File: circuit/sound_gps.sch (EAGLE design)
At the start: 12 parts, among them CON1 MA02-1, IC1 7805TV

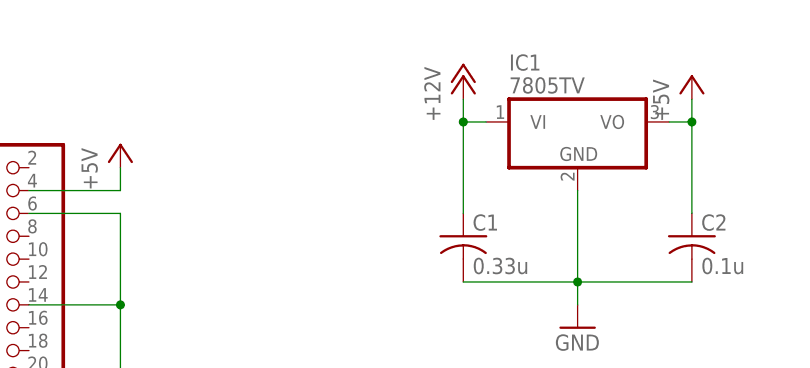
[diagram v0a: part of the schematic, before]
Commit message: スイッチを追加した
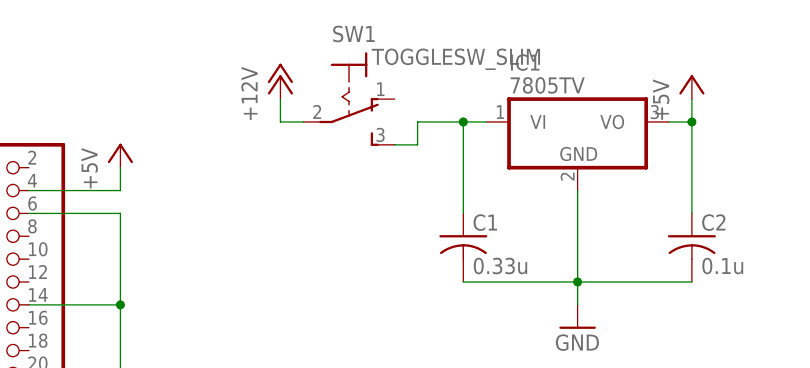
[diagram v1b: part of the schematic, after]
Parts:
- added SW1: TOGGLESW_SLIM, Passive_Robotech:TOGGLESW_SLIM
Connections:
- new net N$3: C1.1, IC1.VI, SW1.S
- net +12V: now also SW1.P; no longer C1.1, IC1.VI
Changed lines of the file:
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@@
 <part name="GND6" library="supply1" deviceset="GND" device=""/>
 <part name="R1" library="Passive_Robotech" deviceset="R" device="-1608" value="10k"/>
+<part name="SW1" library="Passive_Robotech" deviceset="TOGGLESW_SLIM" device=""/>
 </parts>
 <sheets>
@@
 <instance part="JP1" gate="A" x="-66.04" y="45.72"/>
 <instance part="IC1" gate="A1" x="0" y="73.66"/>
-<instance part="P+1" gate="1" x="-12.7" y="78.74"/>
+<instance part="P+1" gate="1" x="-33.02" y="78.74"/>
 <instance part="P+2" gate="1" x="12.7" y="78.74"/>
 <instance part="GND1" gate="1" x="0" y="50.8"/>
@@
 <instance part="GND6" gate="1" x="-27.94" y="10.16"/>
 <instance part="R1" gate="G$1" x="-27.94" y="33.02" rot="R90"/>
+<instance part="SW1" gate="G$1" x="-25.4" y="76.2" rot="R270"/>
 </instances>
 <busses>
@@
 <net name="+12V" class="0">
 <segment>
-<pinref part="P+1" gate="1" pin="+12V"/>
-<wire x1="-12.7" y1="76.2" x2="-12.7" y2="73.66" width="0.1524" layer="91"/>
-<pinref part="IC1" gate="A1" pin="VI"/>
-<wire x1="-12.7" y1="73.66" x2="-10.16" y2="73.66" width="0.1524" layer="91"/>
-<wire x1="-12.7" y1="73.66" x2="-12.7" y2="63.5" width="0.1524" layer="91"/>
-<junction x="-12.7" y="73.66"/>
-<pinref part="C1" gate="G$1" pin="1"/>
-</segment>
-<segment>
 <pinref part="POWER" gate="G$1" pin="3"/>
 <pinref part="P+4" gate="1" pin="+12V"/>
 <wire x1="-60.96" y1="-5.08" x2="-55.88" y2="-5.08" width="0.1524" layer="91"/>
 <wire x1="-55.88" y1="-5.08" x2="-55.88" y2="-2.54" width="0.1524" layer="91"/>
+</segment>
+<segment>
+<pinref part="P+1" gate="1" pin="+12V"/>
+<wire x1="-33.02" y1="76.2" x2="-33.02" y2="73.66" width="0.1524" layer="91"/>
+<pinref part="SW1" gate="G$1" pin="P"/>
+<wire x1="-33.02" y1="73.66" x2="-30.48" y2="73.66" width="0.1524" layer="91"/>
 </segment>
 </net>
@@
 </segment>
 </net>
+<net name="N$3" class="0">
+<segment>
+<pinref part="IC1" gate="A1" pin="VI"/>
+<wire x1="-12.7" y1="73.66" x2="-10.16" y2="73.66" width="0.1524" layer="91"/>
+<wire x1="-12.7" y1="73.66" x2="-12.7" y2="63.5" width="0.1524" layer="91"/>
+<pinref part="C1" gate="G$1" pin="1"/>
+<pinref part="SW1" gate="G$1" pin="S"/>
+<wire x1="-20.32" y1="71.12" x2="-17.78" y2="71.12" width="0.1524" layer="91"/>
+<wire x1="-17.78" y1="71.12" x2="-17.78" y2="73.66" width="0.1524" layer="91"/>
+<wire x1="-17.78" y1="73.66" x2="-12.7" y2="73.66" width="0.1524" layer="91"/>
+<junction x="-12.7" y="73.66"/>
+</segment>
+</net>

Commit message: circuit version 2.0
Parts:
- POWER, SPEAKER: value (none) -> DCJACK-NEW-18742; device con-jack:JACK-PLUG0 -> Connector_Robotech:DCJACK-NEW-18742
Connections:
- net +12V: now also POWER.CENTER; no longer POWER.3
- net AUDIO_NOUT: now also SPEAKER.TIP; no longer SPEAKER.1
- net AUDIO_POUT: now also SPEAKER.CENTER; no longer SPEAKER.3
- net GND: now also POWER.TIP; no longer POWER.1
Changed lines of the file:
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@@
 <part name="GND3" library="supply1" deviceset="GND" device=""/>
 <part name="CON1" library="Connector_Robotech" deviceset="MA02-1" device=""/>
-<part name="POWER" library="con-jack" deviceset="JACK-PLUG" device="0"/>
-<part name="SPEAKER" library="con-jack" deviceset="JACK-PLUG" device="0"/>
 <part name="P+4" library="supply1" deviceset="+12V" device=""/>
 <part name="GND4" library="supply1" deviceset="GND" device=""/>
@@
 <part name="R1" library="Passive_Robotech" deviceset="R" device="-1608" value="10k"/>
 <part name="SW1" library="Passive_Robotech" deviceset="TOGGLESW_SLIM" device=""/>
+<part name="POWER" library="Connector_Robotech" deviceset="DCJACK-NEW" device="-18742"/>
+<part name="SPEAKER" library="Connector_Robotech" deviceset="DCJACK-NEW" device="-18742"/>
 </parts>
 <sheets>
@@
 <instance part="GND3" gate="1" x="50.8" y="0"/>
 <instance part="CON1" gate="G$1" x="-7.62" y="-10.16"/>
-<instance part="POWER" gate="G$1" x="-66.04" y="-7.62"/>
-<instance part="SPEAKER" gate="G$1" x="-66.04" y="-25.4"/>
 <instance part="P+4" gate="1" x="-55.88" y="0"/>
-<instance part="GND4" gate="1" x="-55.88" y="-15.24"/>
+<instance part="GND4" gate="1" x="-68.58" y="-2.54"/>
 <instance part="P+5" gate="1" x="-50.8" y="71.12"/>
 <instance part="GND5" gate="1" x="-50.8" y="10.16"/>
@@
 <instance part="R1" gate="G$1" x="-27.94" y="33.02" rot="R90"/>
 <instance part="SW1" gate="G$1" x="-25.4" y="76.2" rot="R270"/>
+<instance part="POWER" gate="G$1" x="-73.66" y="-10.16"/>
+<instance part="SPEAKER" gate="G$1" x="-73.66" y="-27.94"/>
 </instances>
 <busses>
@@
 <net name="+12V" class="0">
 <segment>
-<pinref part="POWER" gate="G$1" pin="3"/>
 <pinref part="P+4" gate="1" pin="+12V"/>
-<wire x1="-60.96" y1="-5.08" x2="-55.88" y2="-5.08" width="0.1524" layer="91"/>
-<wire x1="-55.88" y1="-5.08" x2="-55.88" y2="-2.54" width="0.1524" layer="91"/>
+<wire x1="-66.04" y1="-10.16" x2="-55.88" y2="-10.16" width="0.1524" layer="91"/>
+<wire x1="-55.88" y1="-10.16" x2="-55.88" y2="-2.54" width="0.1524" layer="91"/>
+<pinref part="POWER" gate="G$1" pin="CENTER"/>
 </segment>
 <segment>
@@
 </segment>
 <segment>
-<pinref part="POWER" gate="G$1" pin="1"/>
 <pinref part="GND4" gate="1" pin="GND"/>
-<wire x1="-60.96" y1="-10.16" x2="-55.88" y2="-10.16" width="0.1524" layer="91"/>
-<wire x1="-55.88" y1="-10.16" x2="-55.88" y2="-12.7" width="0.1524" layer="91"/>
+<wire x1="-73.66" y1="2.54" x2="-68.58" y2="2.54" width="0.1524" layer="91"/>
+<wire x1="-68.58" y1="2.54" x2="-68.58" y2="0" width="0.1524" layer="91"/>
+<pinref part="POWER" gate="G$1" pin="TIP"/>
+<wire x1="-73.66" y1="0" x2="-73.66" y2="2.54" width="0.1524" layer="91"/>
 </segment>
 <segment>
@@
 </segment>
 <segment>
-<pinref part="SPEAKER" gate="G$1" pin="1"/>
-<wire x1="-60.96" y1="-27.94" x2="-53.34" y2="-27.94" width="0.1524" layer="91"/>
-<label x="-58.42" y="-27.94" size="1.778" layer="95"/>
+<wire x1="-73.66" y1="-17.78" x2="-55.88" y2="-17.78" width="0.1524" layer="91"/>
+<label x="-58.42" y="-17.78" size="1.778" layer="95"/>
+<pinref part="SPEAKER" gate="G$1" pin="TIP"/>
 </segment>
 </net>
@@
 </segment>
 <segment>
-<pinref part="SPEAKER" gate="G$1" pin="3"/>
-<wire x1="-60.96" y1="-22.86" x2="-53.34" y2="-22.86" width="0.1524" layer="91"/>
-<label x="-58.42" y="-22.86" size="1.778" layer="95"/>
-</segment>
-</net>
+<wire x1="-66.04" y1="-27.94" x2="-55.88" y2="-27.94" width="0.1524" layer="91"/>
+<label x="-58.42" y="-27.94" size="1.778" layer="95"/>
+<pinref part="SPEAKER" gate="G$1" pin="CENTER"/>
+</segment>
+</net>

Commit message: circuit version 3.0
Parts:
- removed POWER, SPEAKER: DCJACK-NEW-18742, Connector_Robotech:DCJACK-NEW-18742
- added CN1: DCJACK-NEW-18742, Connector_Robotech:DCJACK-NEW-18742
- added J2: DCJACK, Connector_Robotech:DCJACK
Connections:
- net +12V: now also CN1.CENTER; no longer POWER.CENTER
- net AUDIO_NOUT: now also J2.2; no longer SPEAKER.TIP
- net AUDIO_POUT: now also J2.1; no longer SPEAKER.CENTER
- net GND: now also CN1.TIP; no longer POWER.TIP
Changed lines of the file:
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@@
 <part name="R1" library="Passive_Robotech" deviceset="R" device="-1608" value="10k"/>
 <part name="SW1" library="Passive_Robotech" deviceset="TOGGLESW_SLIM" device=""/>
-<part name="POWER" library="Connector_Robotech" deviceset="DCJACK-NEW" device="-18742"/>
-<part name="SPEAKER" library="Connector_Robotech" deviceset="DCJACK-NEW" device="-18742"/>
+<part name="J2" library="Connector_Robotech" deviceset="DCJACK" device=""/>
+<part name="CN1" library="Connector_Robotech" deviceset="DCJACK-NEW" device="-18742"/>
 </parts>
 <sheets>
@@
 <instance part="GND3" gate="1" x="50.8" y="0"/>
 <instance part="CON1" gate="G$1" x="-7.62" y="-10.16"/>
-<instance part="P+4" gate="1" x="-55.88" y="0"/>
-<instance part="GND4" gate="1" x="-68.58" y="-2.54"/>
+<instance part="P+4" gate="1" x="-66.04" y="0"/>
+<instance part="GND4" gate="1" x="-73.66" y="2.54"/>
 <instance part="P+5" gate="1" x="-50.8" y="71.12"/>
 <instance part="GND5" gate="1" x="-50.8" y="10.16"/>
@@
 <instance part="R1" gate="G$1" x="-27.94" y="33.02" rot="R90"/>
 <instance part="SW1" gate="G$1" x="-25.4" y="76.2" rot="R270"/>
-<instance part="POWER" gate="G$1" x="-73.66" y="-10.16"/>
-<instance part="SPEAKER" gate="G$1" x="-73.66" y="-27.94"/>
+<instance part="J2" gate="G$1" x="-73.66" y="-25.4"/>
+<instance part="CN1" gate="G$1" x="-78.74" y="-5.08"/>
 </instances>
 <busses>
@@
 <net name="+12V" class="0">
 <segment>
-<pinref part="P+4" gate="1" pin="+12V"/>
-<wire x1="-66.04" y1="-10.16" x2="-55.88" y2="-10.16" width="0.1524" layer="91"/>
-<wire x1="-55.88" y1="-10.16" x2="-55.88" y2="-2.54" width="0.1524" layer="91"/>
-<pinref part="POWER" gate="G$1" pin="CENTER"/>
-</segment>
-<segment>
 <pinref part="P+1" gate="1" pin="+12V"/>
 <wire x1="-33.02" y1="76.2" x2="-33.02" y2="73.66" width="0.1524" layer="91"/>
 <pinref part="SW1" gate="G$1" pin="P"/>
 <wire x1="-33.02" y1="73.66" x2="-30.48" y2="73.66" width="0.1524" layer="91"/>
+</segment>
+<segment>
+<pinref part="P+4" gate="1" pin="+12V"/>
+<wire x1="-66.04" y1="-2.54" x2="-66.04" y2="-5.08" width="0.1524" layer="91"/>
+<pinref part="CN1" gate="G$1" pin="CENTER"/>
+<wire x1="-66.04" y1="-5.08" x2="-71.12" y2="-5.08" width="0.1524" layer="91"/>
 </segment>
 </net>
@@
 <wire x1="53.34" y1="30.48" x2="50.8" y2="30.48" width="0.1524" layer="91"/>
 <junction x="50.8" y="30.48"/>
-</segment>
-<segment>
-<pinref part="GND4" gate="1" pin="GND"/>
-<wire x1="-73.66" y1="2.54" x2="-68.58" y2="2.54" width="0.1524" layer="91"/>
-<wire x1="-68.58" y1="2.54" x2="-68.58" y2="0" width="0.1524" layer="91"/>
-<pinref part="POWER" gate="G$1" pin="TIP"/>
-<wire x1="-73.66" y1="0" x2="-73.66" y2="2.54" width="0.1524" layer="91"/>
 </segment>
 <segment>
@@
 <wire x1="-27.94" y1="12.7" x2="-27.94" y2="15.24" width="0.1524" layer="91"/>
 </segment>
+<segment>
+<pinref part="GND4" gate="1" pin="GND"/>
+<wire x1="-73.66" y1="5.08" x2="-73.66" y2="7.62" width="0.1524" layer="91"/>
+<wire x1="-73.66" y1="7.62" x2="-78.74" y2="7.62" width="0.1524" layer="91"/>
+<pinref part="CN1" gate="G$1" pin="TIP"/>
+<wire x1="-78.74" y1="5.08" x2="-78.74" y2="7.62" width="0.1524" layer="91"/>
+</segment>
 </net>
 <net name="AUDIO_IN" class="0">
@@
 </segment>
 <segment>
-<wire x1="-73.66" y1="-17.78" x2="-55.88" y2="-17.78" width="0.1524" layer="91"/>
-<label x="-58.42" y="-17.78" size="1.778" layer="95"/>
-<pinref part="SPEAKER" gate="G$1" pin="TIP"/>
+<wire x1="-68.58" y1="-25.4" x2="-58.42" y2="-25.4" width="0.1524" layer="91"/>
+<label x="-60.96" y="-25.4" size="1.778" layer="95"/>
+<pinref part="J2" gate="G$1" pin="2"/>
 </segment>
 </net>
@@
 </segment>
 <segment>
-<wire x1="-66.04" y1="-27.94" x2="-55.88" y2="-27.94" width="0.1524" layer="91"/>
-<label x="-58.42" y="-27.94" size="1.778" layer="95"/>
-<pinref part="SPEAKER" gate="G$1" pin="CENTER"/>
-</segment>
-</net>
+<wire x1="-68.58" y1="-22.86" x2="-58.42" y2="-22.86" width="0.1524" layer="91"/>
+<label x="-60.96" y="-22.86" size="1.778" layer="95"/>
+<pinref part="J2" gate="G$1" pin="1"/>
+</segment>
+</net>
